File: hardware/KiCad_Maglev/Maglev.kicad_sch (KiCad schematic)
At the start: 0 parts

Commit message: added first version of logic design with parts of power driver circuit
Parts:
- added BOOT1, RESET1: 430182043816, Switch_SMD_Wurth:SW_Wurth_WS-TASV_430182043816, symbol Switch_Wurth_WS-TASV:430182043816
- added C2: 0805_H1.25_R_885012107015, Capacitor_SMD_Wurth:C_Wurth_WCAP-CSGP-0805_H1.25_R, symbol Capacitor_Wurth_WCAP-CSGP:0805_H1.25_R_885012107015
- added D1: 824011, SOT95P280X116-5N, symbol 824011:824011
- added J1: USB_C_Receptacle, WURTH_USB:632723300011, symbol Connector:USB_C_Receptacle_USB2.0
- added J2: 62100421921, Connector_SMD_Wurth:J_Wurth_WR-PHD_62100421921, symbol Connector_Wurth_WR-PHD:62100421921
- added J3: 61300311121, Connector_THT_Wurth:J_Wurth_WR-PHD_61300311121, symbol Connector_Wurth_WR-PHD:61300311121
- added J4: 694106301002, Connector_THT_Wurth:J_Wurth_WR-DC_694106301002, symbol Connector_Wurth_WR-DC:694106301002
- added L3, L4, L6, L7: 1212_7449152111, Inductor_SMD_Wurth:L_Wurth_WE-ACHC-1212_7449152111, symbol Inductor_Wurth_WE-ACHC:1212_7449152111
- added R1, R2: 0805_R_560112120019, Resistor_SMD_Wurth:R_Wurth_WRIS-RSKS-0805_R, symbol Resistor_Wurth_WRIS-RSKS:0805_R_560112120019
- added R3, R4: 0402_560112110020, Resistor_SMD_Wurth:R_Wurth_WRIS-RSKS-0402, symbol Resistor_Wurth_WRIS-RSKS:0402_560112110020
- added U1: ESP32-C3, ESP32-C3FH4:QFN50P500X500X90-33N, symbol MCU_Espressif:ESP32-C3
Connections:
- new net: D1.3 (I/O1), J1.A7 (D-), J1.B7 (D-)
- new net: D1.4 (I/O2), J1.A6 (D+), J1.B6 (D+)
- new net: J1.A5 (CC1), R2.1
- new net: J1.B5 (CC2), R1.1
- new net: J2.3, U1.27 (U0RXD/GPIO20)
- new net: J2.1, U1.28 (U0TXD/GPIO21)
- new net +3.3V: R3.1, R4.1
- new net +USB_D: D1.4 (I/O2), U1.25 (GPIO18/USB_D-)
- new net -USB_D: D1.3 (I/O1), U1.26 (GPIO19/USB_D+)
- new net 40 MHz Oscillator/+XTAL_40MHz: U1.30 (XTAL_P)
- new net 40 MHz Oscillator/-XTAL_40MHz: U1.29 (XTAL_N)
- new net BOOT: BOOT1.1, BOOT1.3, R4.2, U1.15 (GPIO9/BOOT)
- new net CHIP_EN: C2.1, R3.2, RESET1.1, RESET1.3, U1.7 (CHIP_EN)
- new net ESP32 Power Circuit/VDD3P3: U1.2 (VDD3P3), U1.3 (VDD3P3)
- new net ESP32 Power Circuit/VDD3P3_CPU: U1.17 (VDD3P3_CPU)
- new net ESP32 Power Circuit/VDD3P3_RTC: U1.11 (VDD3P3_RTC)
- new net ESP32 Power Circuit/VDDA: U1.31 (VDDA), U1.32 (VDDA)
- new net Electromagnet Driver/EM_A_N: L4.2
- new net Electromagnet Driver/EM_A_P: L4.1
- new net Electromagnet Driver/EM_B_N: L3.2
- new net Electromagnet Driver/EM_B_P: L3.1
- new net Electromagnet Driver/EM_C_N: L6.2
- new net Electromagnet Driver/EM_C_P: L6.1
- new net Electromagnet Driver/EM_D_N: L7.2
- new net Electromagnet Driver/EM_D_P: L7.1
- new net GND: BOOT1.2, BOOT1.4, C2.2, D1.2 (GND), J1.A1 (GND), J1.A12 (GND), J1.B1 (GND), J1.B12 (GND), J1.S1 (SHIELD), J3.1, J3.2, J3.3, J4.1, J4.2, J4.3, R1.2, R2.2, RESET1.2, RESET1.4, U1.33 (GND)
- new net HBRIDGE_ALL_EN: U1.12 (MTCK/GPIO6)
- new net HBRIDGE_A_DIR: U1.23 (SPID/GPIO16)
- new net HBRIDGE_A_ISENSE: U1.4 (XTAL_32K_P/ADC1_CH0)
- new net HBRIDGE_A_PWM: U1.24 (SPIQ/GPIO17)
- new net HBRIDGE_B_DIR: U1.21 (SPICS0/GPIO14)
- new net HBRIDGE_B_ISENSE: U1.5 (XTAL_32K_N/ADC1_CH1)
- new net HBRIDGE_B_PWM: U1.22 (SPICLK/GPIO15)
- new net HBRIDGE_C_DIR: U1.19 (SPIHD/GPIO12)
- new net HBRIDGE_C_ISENSE: U1.6 (GPIO2/ADC1_CH2)
- new net HBRIDGE_C_PWM: U1.20 (SPIWP/GPIO13)
- new net HBRIDGE_D_DIR: U1.10 (MTDI/GPIO5/ADC2_CH0)
- new net HBRIDGE_D_ISENSE: U1.8 (GPIO3/ADC1_CH3)
- new net HBRIDGE_D_PWM: U1.9 (MTMS/GPIO4/ADC1_CH4)
- new net HBRIDG_ALL_FAULT: U1.13 (MTDO/GPIO7)
- new net I2C_INT: U1.18 (VDD_SPI/GPIO11)
- new net I2C_SCL: U1.16 (GPIO10)
- new net I2C_SDA: U1.14 (GPIO8)
- new net RXD: J2.4
- new net TXD: J2.2
- new net USB Power Circuit/USB_VBUS: D1.5 (VDD), J1.A4 (VBUS), J1.A9 (VBUS), J1.B4 (VBUS), J1.B9 (VBUS)
- no-connect marks 0 -> 3
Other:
- added sheet 3D Hall Sensor (3d_hall_sensor.kicad_sch)
- added sheet 40 MHz Oscillator (40MHz_oscillator.kicad_sch)
- added sheet ESP32 Power Circuit (esp32_power_circuit.kicad_sch)
- added sheet Electromagnet Driver (electromagnet_driver.kicad_sch)
- added sheet USB Power Circuit (usb_power_circuit.kicad_sch)
- note added: "Inductors as places holder for Elektro-Magnet"
- note added: "Pin Header Interface (place holder) tbd. (Felix)"
- note added: "Power Connect tbd. (Denz)"
- note added: "RESET and BOOT Buttons"
- note added: "USB-C Connector"

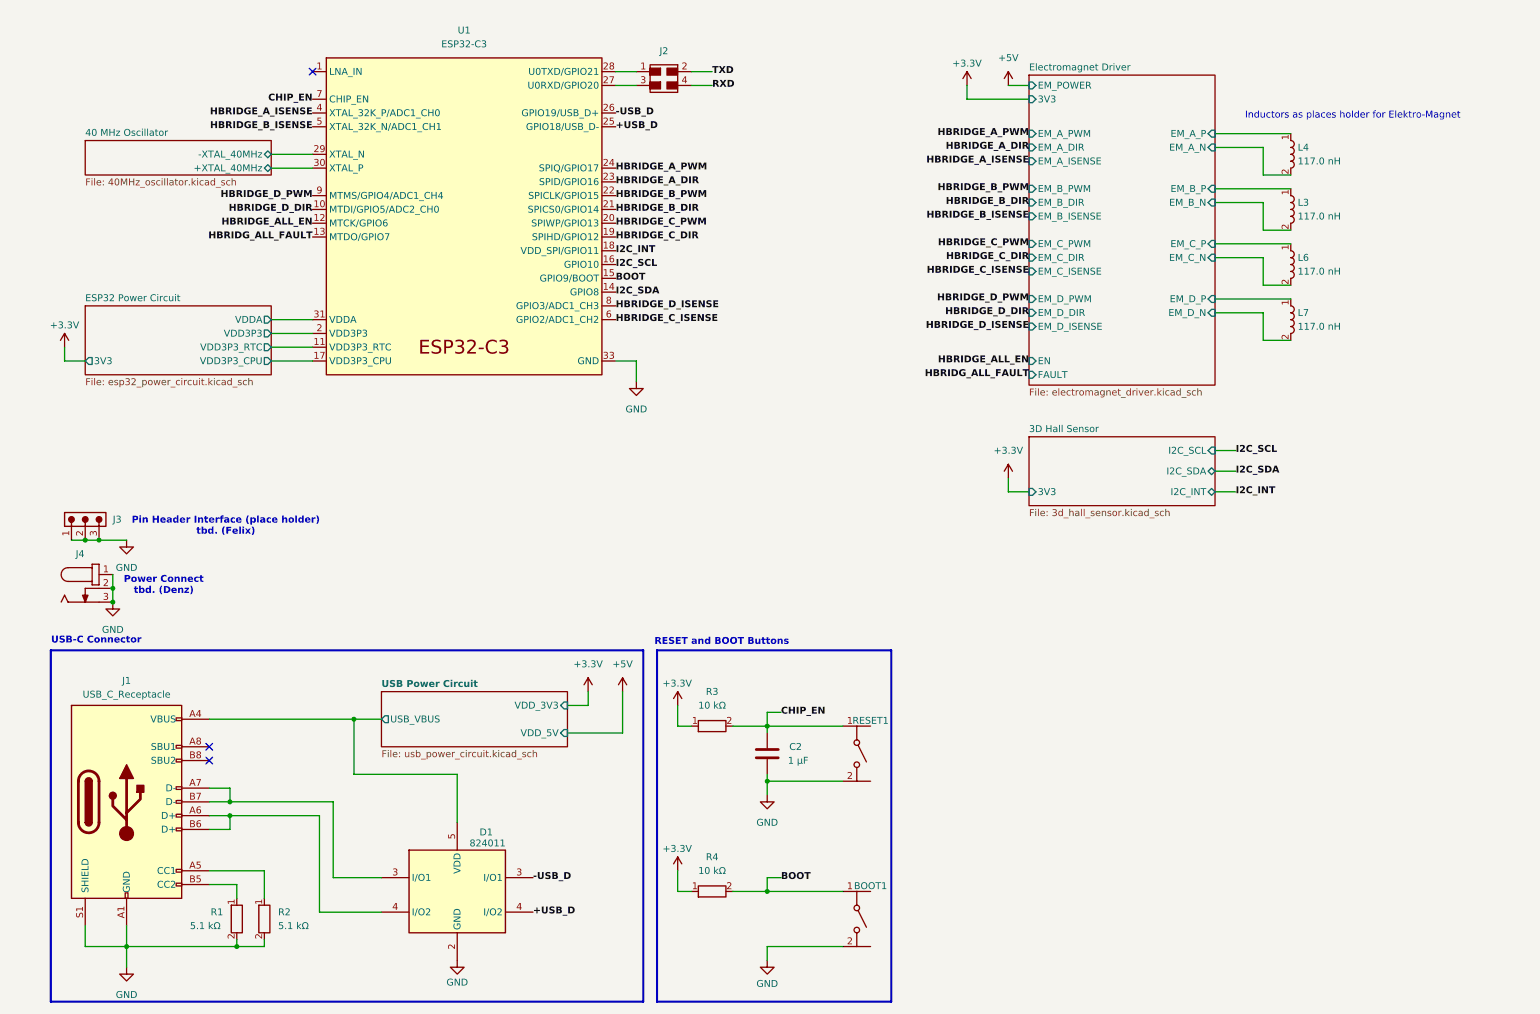
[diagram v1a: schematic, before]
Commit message: some changes to pcb schmatic, added datasheets for used components and linked wurth repo
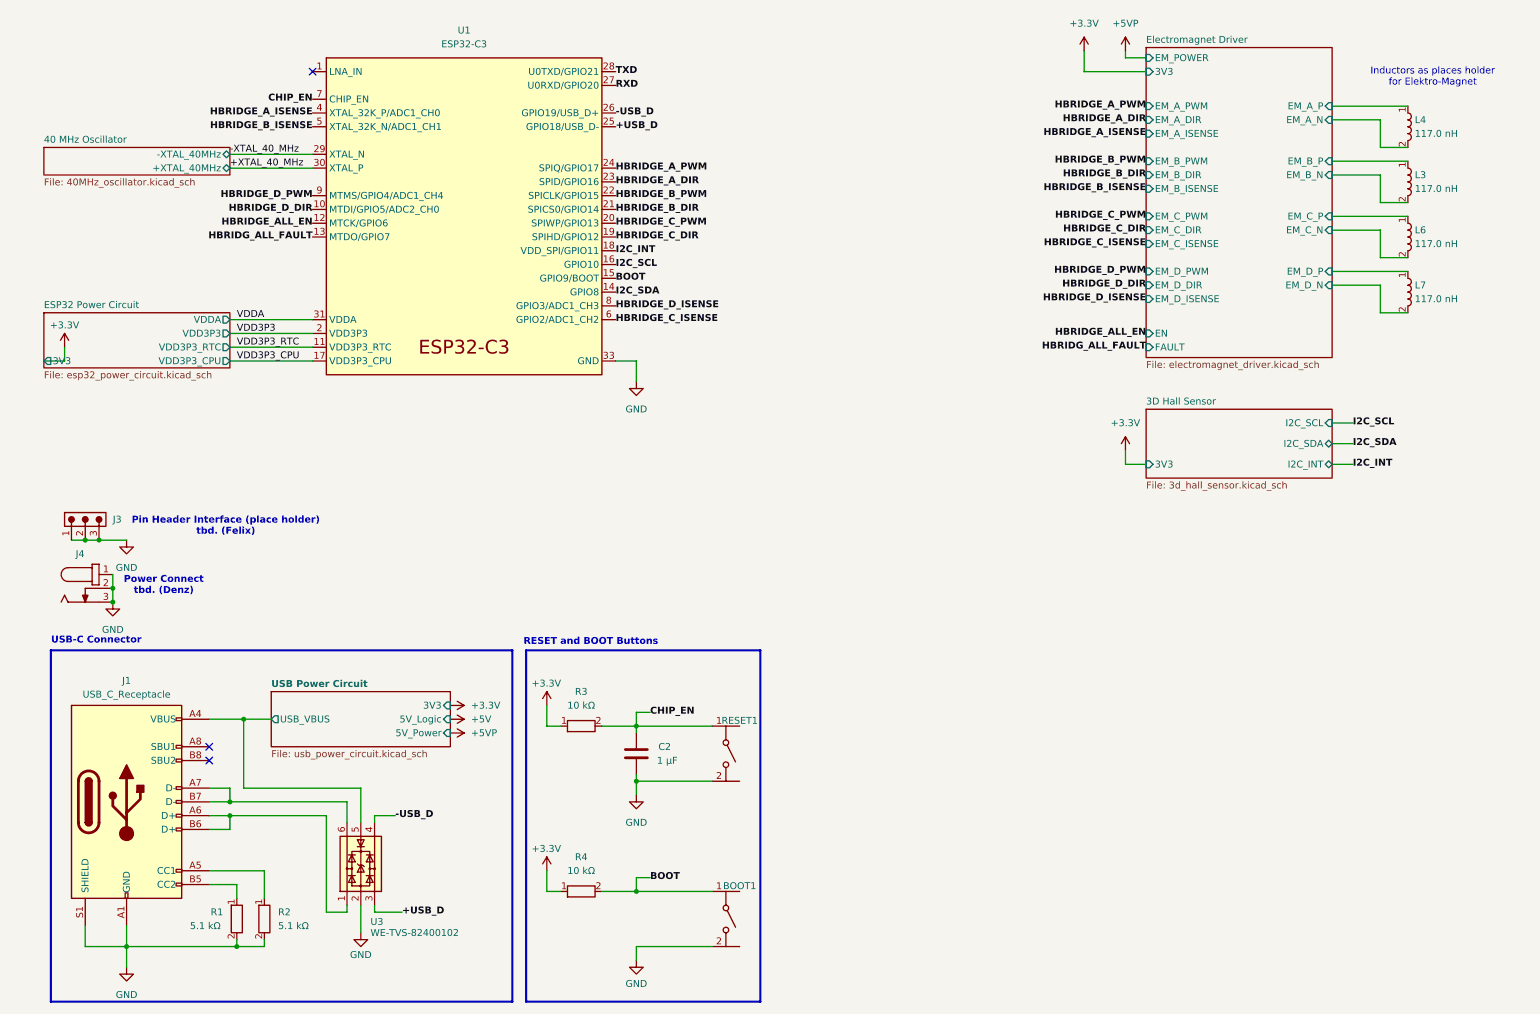
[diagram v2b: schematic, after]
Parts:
- removed D1: 824011, SOT95P280X116-5N, symbol 824011:824011
- removed J2: 62100421921, Connector_SMD_Wurth:J_Wurth_WR-PHD_62100421921, symbol Connector_Wurth_WR-PHD:62100421921
- added U3: WE-TVS-82400102, SOT95P280X116-6N:SOT95P280X116-6N, symbol Power_Protection:WE-TVS-82400102
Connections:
- net +USB_D: now also U3.3
- net -USB_D: now also U3.4
- net GND: now also U3.2
- net RXD: now also U1.27 (U0RXD/GPIO20)
- net TXD: now also U1.28 (U0TXD/GPIO21)
- net USB Power Circuit/USB_VBUS: now also U3.5
- net at J1.A7 (D-), J1.B7 (D-): now also U3.6
- net at J1.A6 (D+), J1.B6 (D+): now also U3.1
- net 40 MHz Oscillator/+XTAL_40MHz renamed +XTAL_40_MHz
- net 40 MHz Oscillator/-XTAL_40MHz renamed -XTAL_40_MHz
- net ESP32 Power Circuit/VDD3P3 renamed VDD3P3
- net ESP32 Power Circuit/VDD3P3_CPU renamed VDD3P3_CPU
- net ESP32 Power Circuit/VDD3P3_RTC renamed VDD3P3_RTC
- net ESP32 Power Circuit/VDDA renamed VDDA
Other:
- sheet USB Power Circuit ports: added 3V3, 5V_Logic, 5V_Power; removed VDD_3V3, VDD_5V
- moved on the sheet: BOOT1, C2, L3, L4, L6, L7, R3, R4, RESET1

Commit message: Added Pin header
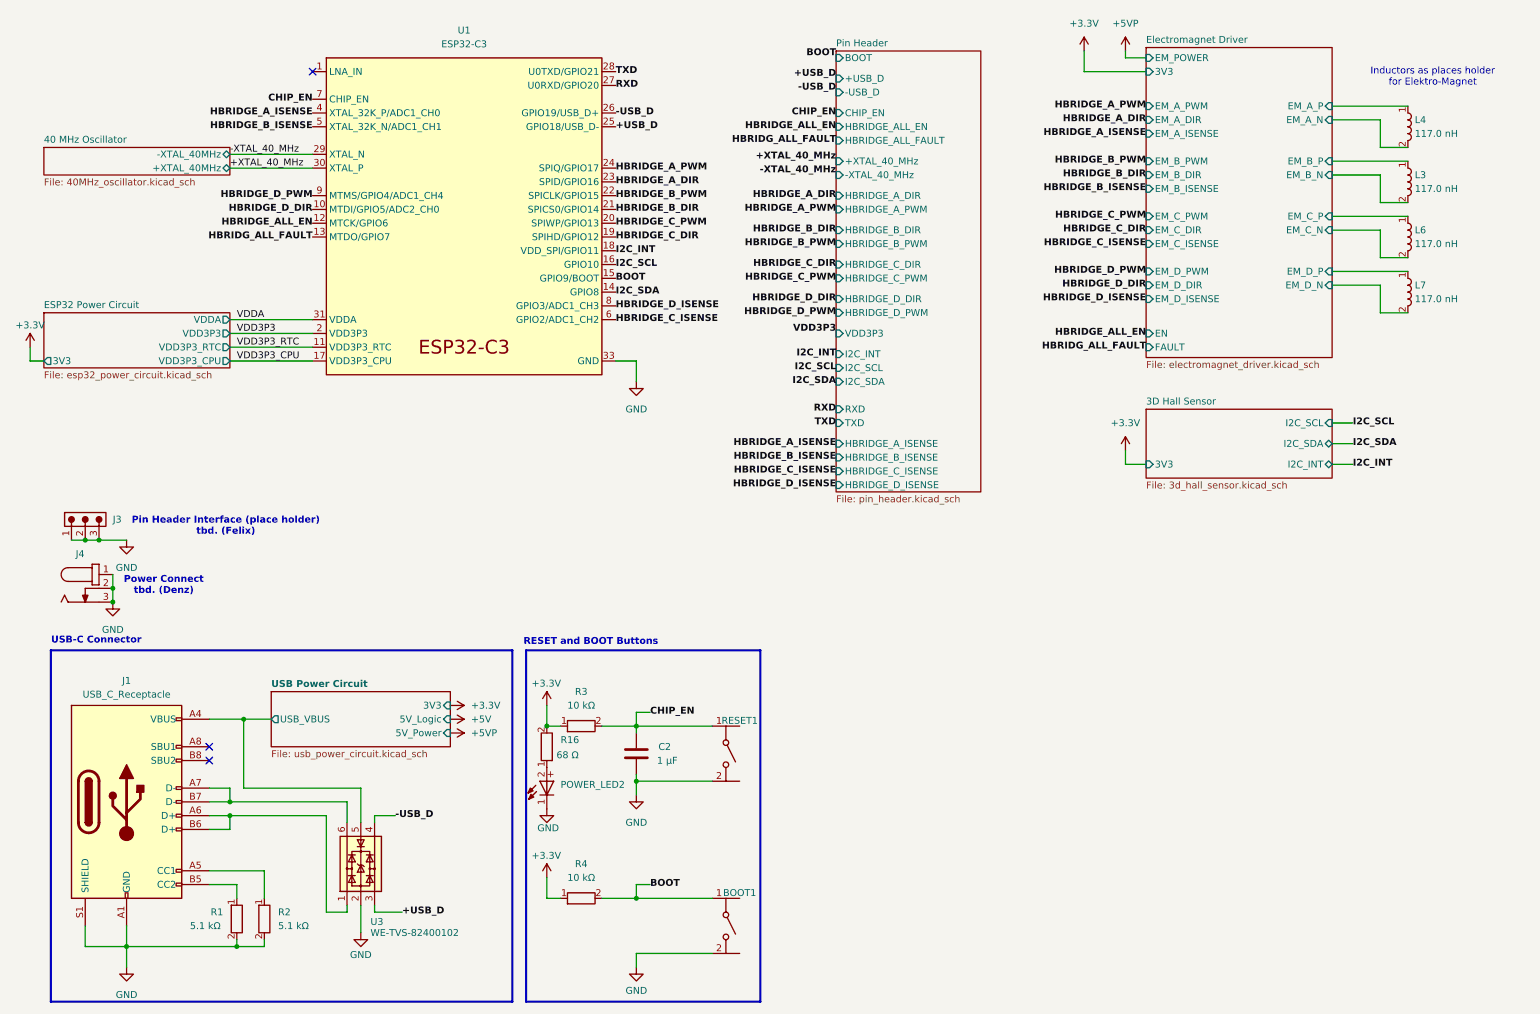
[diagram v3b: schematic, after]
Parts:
- added POWER_LED2: 0603dome_150060VS86000, LED_SMD_Wurth:D_Wurth_WL-SMCW-0603dome, symbol LED_Wurth_WL-SMCW:0603dome_150060VS86000
- added R16: 1206_R_560112132050, Resistor_SMD_Wurth:R_Wurth_WRIS-RSKS-1206_R, symbol Resistor_Wurth_WRIS-RSKS:1206_R_560112132050
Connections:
- net +3.3V: now also R16.2
- net GND: now also POWER_LED2.1 (-)
- new net: POWER_LED2.2 (+), R16.1
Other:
- added sheet Pin Header (pin_header.kicad_sch)
- moved on the sheet: BOOT1, R4

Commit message: Adde StatusLED, Jumper Power Voltage
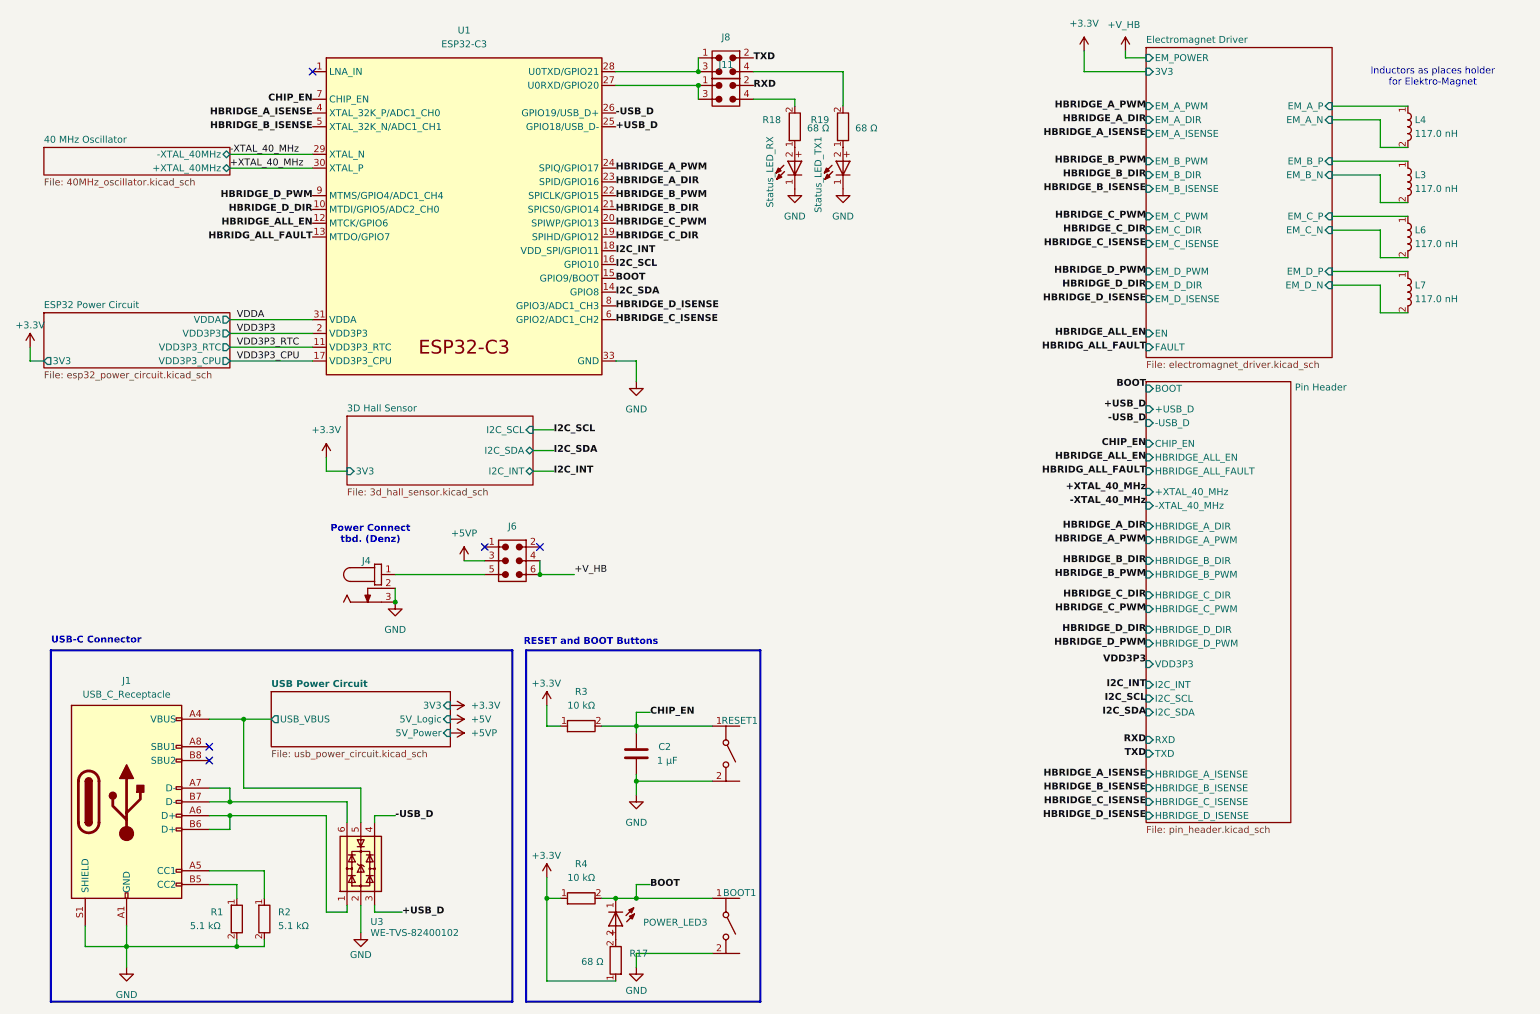
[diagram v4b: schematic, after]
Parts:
- removed J3: 61300311121, Connector_THT_Wurth:J_Wurth_WR-PHD_61300311121, symbol Connector_Wurth_WR-PHD:61300311121
- removed POWER_LED2: 0603dome_150060VS86000, LED_SMD_Wurth:D_Wurth_WL-SMCW-0603dome, symbol LED_Wurth_WL-SMCW:0603dome_150060VS86000
- removed R16: 1206_R_560112132050, Resistor_SMD_Wurth:R_Wurth_WRIS-RSKS-1206_R, symbol Resistor_Wurth_WRIS-RSKS:1206_R_560112132050
- added J11, J8: 61300421121, Connector_THT_Wurth:J_Wurth_WR-PHD_61300421121, symbol Connector_Wurth_WR-PHD:61300421121
- added J6: 61300621121, Connector_THT_Wurth:J_Wurth_WR-PHD_61300621121, symbol Connector_Wurth_WR-PHD:61300621121
- added POWER_LED3, Status_LED_RX, Status_LED_TX1: 0603dome_150060VS86000, LED_SMD_Wurth:D_Wurth_WL-SMCW-0603dome, symbol LED_Wurth_WL-SMCW:0603dome_150060VS86000
- added R17, R18, R19: 1206_R_560112132050, Resistor_SMD_Wurth:R_Wurth_WRIS-RSKS-1206_R, symbol Resistor_Wurth_WRIS-RSKS:1206_R_560112132050
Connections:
- net +3.3V: now also R17.1
- net +5VP: now also J6.3
- net BOOT: now also POWER_LED3.1 (-)
- net GND: now also Status_LED_RX.1 (-), Status_LED_TX1.1 (-); no longer J4.1
- net RXD: now also J11.2; no longer U1.27 (U0RXD/GPIO20)
- net TXD: now also J8.2; no longer U1.28 (U0TXD/GPIO21)
- new net: POWER_LED3.2 (+), R17.2
- new net: J11.1, J11.3, U1.27 (U0RXD/GPIO20)
- new net: J11.4, R18.2
- new net: J8.1, J8.3, U1.28 (U0TXD/GPIO21)
- new net: J8.4, R19.2
- new net: J4.1, J6.5
- new net: R18.1, Status_LED_RX.2 (+)
- new net: R19.1, Status_LED_TX1.2 (+)
- new net +V_HB: J6.4, J6.6
- no-connect marks 3 -> 5
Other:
- note removed: "Pin Header Interface (place holder) tbd. (Felix)"
